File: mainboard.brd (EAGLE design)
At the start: 90.2 x 95.9 mm, 160 parts, among them IC1 LM234Z, J1 1981584-1, J2 POWER_JACKPTH_LOCK, Q1 IRLML5103, Q2 IRLML5103, Q3 IRLML5103, Q4 IRLML5103, Q5 IRLML5103, T1 NDS352A, T2 NDS352A, T3 NDS352A, T4 NDS352A, T5 NDS352A, U1 RFM23BP, U10 EP2W+, U11 S1216V8, U12 Value, U2 LSM9DS1, U3 MAX708RESA-T, U4 ATSAMD21G-A, U5 MAX4372TEUK+T, U6 MAX4372TEUK+T, U7 TPS54226PWPRPWP14_2P31X2P46-L, U8 LTC4121-4.2, U9 LC05111C13MTTTG, X1 BU-SMA-V, X2 BU-SMA-V, X3 BU-SMA-V, Y1 32.768kHz

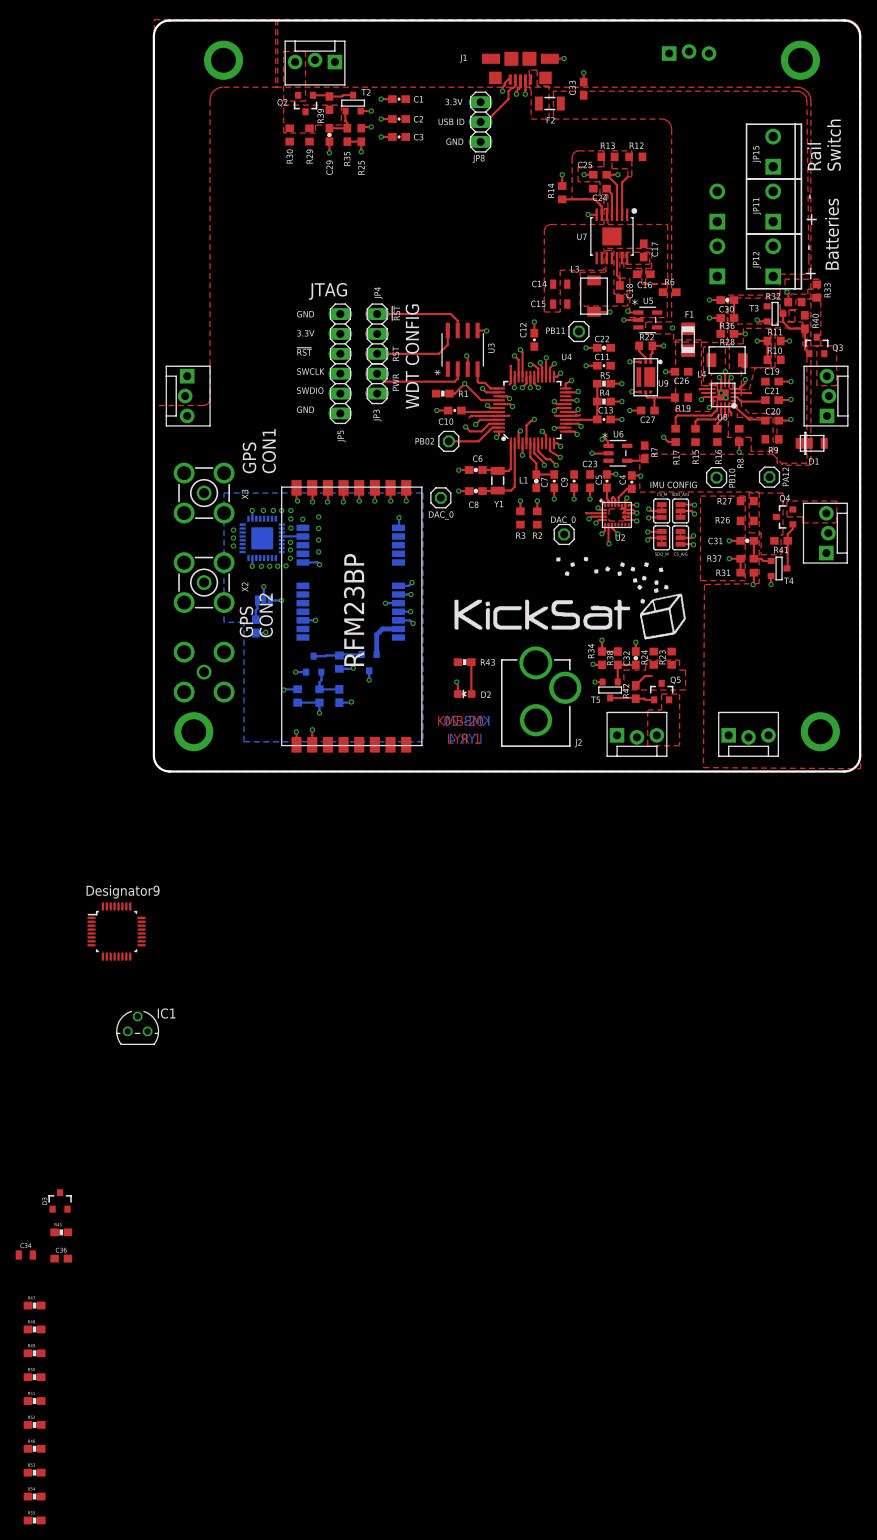
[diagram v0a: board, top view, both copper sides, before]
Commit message: Latest kicksat2 mainboard update (KMB-21). New from KMB-20: MRAM, power relays, microSD card, 2 spots for [XLab Tester Boards](https://github.com/maholli/XTB)
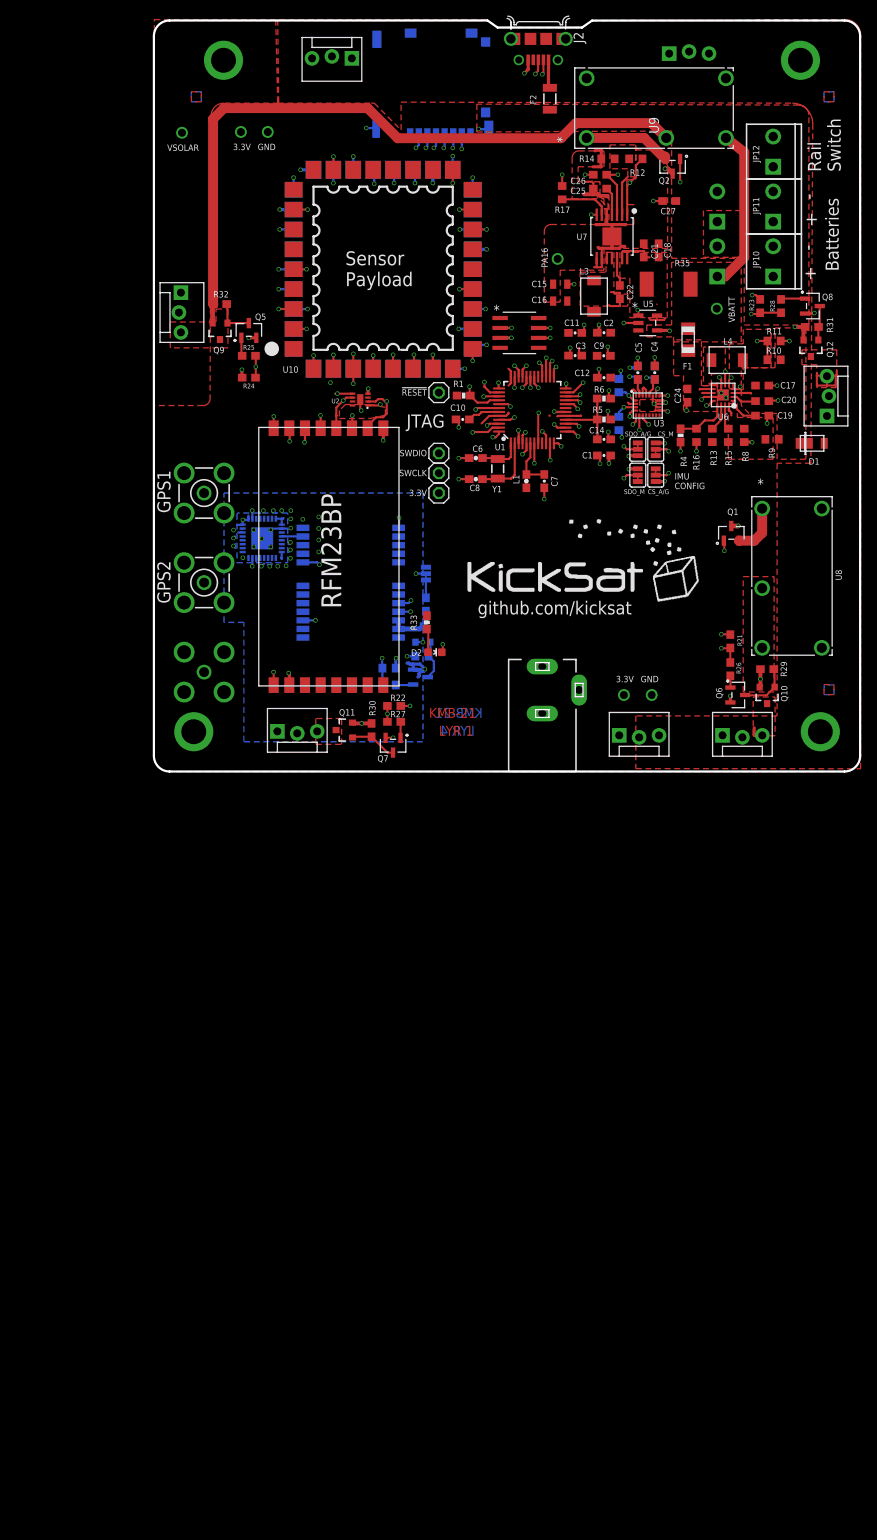
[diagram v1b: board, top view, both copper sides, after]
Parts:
- removed C28: 0.1uF, SparkFun-Capacitors:0603
- removed C29, C30, C31, C32: .1uF, SparkFun-Capacitors:0603-CAP@1
- removed C33: 2.2uF, SparkFun-Capacitors:0603
- removed C34: 0.33µF, SparkFun-Capacitors:0805
- removed C36: 10uF, SparkFun-Capacitors:0603
- removed D3: 200mA/70V, SparkFun-DiscreteSemi:SOT23-3
- removed IC1: LM234Z, linear:TO92
- removed JP18: M023.5MM_LOCK, SparkFun-Connectors:SCREWTERMINAL-3.5MM-2_LOCK
- removed JP19, JP20, JP21: (no value), SparkFun-Passives:PAD-JUMPER-3-2OF3_NC_BY_TRACE_YES_SILK_FULL_BOX
- removed JP22, JP28: (no value), pinhead:1X01
- removed JP7: (no value), SparkFun-Connectors:MOLEX-1X3_LOCK
- removed R36, R37, R38: 10k, SparkFun-Resistors:0603
- removed R39, R40, R41, R42: 3.3k, SparkFun-Resistors:0603
- removed R43, R45: 330, SparkFun-Resistors:0603-RES
- removed R44, R46, R47, R48, R49, R50, R51, R52, R53, R54, R55: 10K, SparkFun-Resistors:0603-RES
- removed R7: (no value), SparkFun-Resistors:0603
- removed T1, T2, T3, T4, T5: NDS352A, zetex:SOT-23
- added 3.3V: (no value), pinhead:1X01
- added J3: DCJ0303, maholli:DCJ0303
- added Q10, Q11, Q12, Q9: IRLML5103, User-Submitted:SOT23-3
- added Q6, Q7, Q8: IRLML2803, maholli:SOT-23
- added U13: RFM23BP, RFM23BP:RFM23BP
- added U14: S1216V8, maholli:S1216_24PIN_PACKAGE
- C14: value 22uF -> 0.1uF; device SparkFun-Capacitors:0805 -> SparkFun-Capacitors:0603-CAP
- C16: value 10uF -> 22uF; device SparkFun-Capacitors:0603 -> SparkFun-Capacitors:0805
- C18: value 1.0uF -> 10uF
- C19: value 10uF -> 2.2uF
- C20: value 2.2uF -> 2.2nF
- C21: value 2.2nF -> 10uF
- C22: value .1uF -> 0.1uF; device SparkFun-Capacitors:0603-CAP@1 -> SparkFun-Capacitors:0603
- C23: value 0.1uF -> .1uF; device SparkFun-Capacitors:0603 -> SparkFun-Capacitors:0603-CAP@1
- C24: value 3.3nF -> 22uF
- C25: value 1.0uF -> 3.3nF
- C26: value 22uF -> 1.0uF
- C27: value 0.1uF -> 2.2uF
- J1: value 1981584-1 -> 503182-1852; device audio amplifier example:1981584-1 -> maholli:MOLEX_503182-1852
- J2: value POWER_JACKPTH_LOCK -> 10118194-0001LF; device SparkFun-Connectors:POWER_JACK_PTH_LOCK -> 10118194-0001LF:FRAMATOME_10118194-0001LF
- JP10, JP13: value (none) -> M023.5MM_LOCK; device SparkFun-Connectors:MOLEX-1X3_LOCK -> SparkFun-Connectors:SCREWTERMINAL-3.5MM-2_LOCK
- JP15: value M023.5MM_LOCK -> (none); device SparkFun-Connectors:SCREWTERMINAL-3.5MM-2_LOCK -> SparkFun-Connectors:MOLEX-1X3_LOCK
- JP24: device pinhead:1X01 -> SparkFun-Passives:PAD-JUMPER-3-2OF3_NC_BY_TRACE_YES_SILK_FULL_BOX
- JP3: device pinhead:1X02 -> SparkFun-Passives:PAD-JUMPER-3-2OF3_NC_BY_TRACE_YES_SILK_FULL_BOX
- JP4: device pinhead:1X03 -> SparkFun-Passives:PAD-JUMPER-3-2OF3_NC_BY_TRACE_YES_SILK_FULL_BOX
- JP5: device pinhead:1X06 -> SparkFun-Connectors:MOLEX-1X3_LOCK
- JP8: device pinhead:1X03 -> SparkFun-Connectors:MOLEX-1X3_LOCK
- Q1, Q2, Q3, Q5: value IRLML5103 -> IRLML2803; device User-Submitted:SOT23-3 -> maholli:SOT-23
- R13: value 22.1 -> 470k
- R14: value 100K -> 22.1k
- R15: value 470k -> 4.7k
- R16: value 4.7k -> 6.04K
- R17: value 6.04K -> 100K
- R18: value 4.7K -> 10K
- R19: value 680 -> 4.7K
- R20: value 10K -> 3.3K
- R21: value 3.3K -> 10k; device resistor:R0603 -> SparkFun-Resistors:0603
- R22: value 1k -> 10k; device resistor:R0603 -> SparkFun-Resistors:0603
- R23, R24: value 4 -> 10k; device resistor:R0603 -> SparkFun-Resistors:0603
- R26, R27: value 4 -> 4.7k; device resistor:R0603 -> SparkFun-Resistors:0603
- R29, R30, R32: value 4 -> 100k; device resistor:R0603 -> SparkFun-Resistors:0603
- R31: value 4.7k -> 100k
- R33: value 4 -> 330; device resistor:R0603 -> SparkFun-Resistors:0603-RES
- R34: value 4.7k -> 10K; device SparkFun-Resistors:0603 -> SparkFun-Resistors:0603-RES
- R35: value 10k -> 0.025; device SparkFun-Resistors:0603 -> resistor:R2512
- R4: value 110K -> 10k
- R5: value 316K -> 110K
- R6: value (none) -> 316K; device SparkFun-Resistors:0603 -> SparkFun-Resistors:0603-RES
- U1: value RFM23BP -> MAX706R; device RFM23BP:RFM23BP -> maholli:SO8
- U10: value EP2W+ -> XTB_2018_04_25; device maholli:QFN32-5X5MM -> maholli:XTB_MEZ
- U11: value S1216V8 -> XTB_2018_04_25; device maholli:S1216_24PIN_PACKAGE -> maholli:XTB_MEZ
- U12: value Value -> EP2W+; device maholli:PBS0032A_N -> maholli:QFN32-5X5MM
- U2: value LSM9DS1 -> MR25H40; device SparkFun-Sensors:LGA24-8X4 -> maholli:DFN-8
- U3: value MAX708RESA-T -> LSM9DS1; device maholli:SO8 -> SparkFun-Sensors:LGA24-8X4
- U6: value MAX4372TEUK+T -> LTC4121-4.2; device maholli:21-0057F -> BrownSpaceEngineering:QFN-16-PAD
- U8: value LTC4121-4.2 -> PE014006; device BrownSpaceEngineering:QFN-16-PAD -> maholli:RELAY5-PE_CO
- U9: value LC05111C13MTTTG -> PE014006; device BrownSpaceEngineering:WDFN6 -> maholli:RELAY5-PE_CO
- moved FRAME1 128.9 mm to (-4.83, 87.1)
- moved FRAME2 128.9 mm to (-4.52, 78.2)
- moved FRAME3 128.9 mm to (-4.83, 60.5)
- moved FRAME4 128.9 mm to (-4.83, 69.3)
- moved J2 93.5 mm to (49.0, 93.5), turned to 180 degrees
- moved R29 89.8 mm to (78.2, 13.1), turned to 180 degrees
- moved JP8 84.3 mm to (72.5, 4.50), turned to 0 degrees
- moved R30 76.7 mm to (27.7, 5.30), turned to 90 degrees
- moved R32 73.4 mm to (8.38, 59.7)
- moved Q5 70.1 mm to (12.1, 56.4)
- moved Q3 65.9 mm to (34.0, 12.1), flipped to the bottom, turned to 90 degrees
- moved R33 65.3 mm to (34.8, 19.1)
- moved R24 62.9 mm to (12.1, 50.3), turned to 180 degrees
- moved JP5 62.6 mm to (86.0, 45.4), turned to 90 degrees
- moved R22 56.1 mm to (30.6, 8.38), turned to 0 degrees
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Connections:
- net PA04 renamed N$22
- removed net 3.3V_REF: U12.30
- removed net A_3.3V: U12.26
- removed net DAC_0: JP22.1, U4.3
- removed net GPS_PWR: Q1.2, U11.23
- removed net I_SOLAR: U4.13, U6.2
- removed net LED_GRN: D2.C, U4.7
- removed net N$22 (its old number): J2.GND, J2.GNDBREAK, JP11.2, JP12.2, JP15.1
- removed net N$27: R48.1, U12.6
- removed net N$41: C27.1, R19.1, U9.P$5
- removed net N$42: C17.1, U7.14
- removed net N$45: R22.2, U9.P$2
- removed net N$48: R51.1, U12.3
- removed net N$50: R46.1, U12.22
- removed net N$56: R55.1, U12.19
- removed net N_ENAB_REG: U4.25, U7.7
- removed net PA12: JP24.1, U4.21
- removed net PA15: U4.24
- removed net PB02: JP28.1, U4.47
- removed net PB09: JP27.1, U4.8
- removed net PB10: JP26.1, U4.19
- removed net PB11: JP25.1, U4.20
- removed net PB13: U4.22
- removed net PWR_GND: C14.1, C15.1, C16.2, C17.2, C24.2, C25.2, R13.1, U7.15, U7.5, U7.8, U7.9
- removed net SPI_SS: U1.NSEL, U4.41
- removed net SPI_SS2: U12.9
- removed net USB_D_N: J1.2, U4.33
- removed net USB_D_P: J1.3, U4.34
- removed net USB_ID: J1.4, JP8.2
- removed net VBURN_IN: Q2.3, Q3.3, Q4.3, Q5.3, R23.1, R24.1, R26.1, R27.1, R29.1, R30.1, R32.1, R33.1, R39.2, R40.2, R41.2, R42.2
- removed net WDT_!PFO: U3.5, U4.29
- removed net WDT_!RESET: JP4.1, U3.7
- removed net WDT_PFI: U3.4, U4.37
- removed net WDT_RESET: JP4.3, U3.8
- new net BURN_RELAY_A: Q2.1, U4.24
- new net BURN_RELAY_B: Q1.1, U4.15
- new net GPS_PWR_IN: Q4.3, R34.2, U14.22, U14.23
- new net LED_1: D2.C, U4.12
- new net SPI_CS_MRAM: U2.P$1
- new net SPI_CS_RFM: U13.NSEL, U4.41
- new net SPI_CS_SD: J1.2, U4.38
- new net SPI_CS_XTB1: U10.P$32, U4.39
- new net SPI_CS_XTB2: U11.P$32, U4.8
- new net USB_D+: J2.3, U4.34
- new net USB_D-: J2.2, U4.33
- new net VBATT_IN: C27.1, F2.2, JP10.1, JP11.1, JP13.2
- new net VBURN_A_IN: Q12.2, Q9.2, R31.2, R32.2, U9.11
- new net VBURN_B_IN: Q10.2, Q11.2, R29.2, R30.2, U8.11
- new net WDT_PWR: U1.2
- new net WDT_WDI: U1.6, U4.28
- new net XTB_RESET: U10.P$26, U11.P$26, U4.37
- new net XTB_START: U10.P$33, U11.P$33, U4.47
- net !RESET: now also JP27.1, U1.7; no longer JP4.2, JP5.3
- net 3.3V: now also 3.3V.1, C13.1, C16.2, J1.4, JP3.3, JP4.3, Q4.2, R13.2, R20.1, U10.P$1, U10.P$18, U10.P$20, U10.P$24, U10.P$27, U10.P$3, U10.P$6, U10.P$7, U11.P$1, U11.P$18, U11.P$20, U11.P$24, U11.P$27, U11.P$3, U11.P$6, U11.P$7, U13.VCC, U3.1, U3.22, U3.23, U3.3; no longer C14.2, C22.1, JP20.3, JP21.3, JP3.2, JP5.2, JP8.1, Q1.3, R16.2, R21.1, R23.2, R24.2, R26.2, R27.2, R29.2, R30.2, R32.2, R43.2, R44.2, R7.1, U1.VCC, U11.22, U12.15, U12.16, U2.1, U2.22, U2.23, U2.3, U6.3, U6.5
- net ENAB_BURN1: now also R24.1, U4.48; no longer R35.1, U4.38
- net ENAB_BURN2: now also R23.1; no longer R36.1
- net ENAB_BURN3: now also R22.1, R27.2, U4.14; no longer R31.2, R37.1, U4.11
- net ENAB_BURN4: now also R21.1, R26.2, U4.13; no longer R34.2, R38.1, U4.12
- net ENAB_GPS: now also R19.1, U4.11; no longer R20.2, U4.39
- net GND: now also C14.2, C15.1, C16.1, C17.2, C18.2, C21.2, C24.2, C25.2, J1.6, J1.P1, J1.P2, J1.P3, J1.P4, J1.P5, J2.5, JP12.2, JP15.1, JP24.1, JP3.1, JP4.1, JP8.1, Q3.2, Q5.2, Q6.2, Q7.2, Q8.2, R14.1, R16.1, R21.2, R22.2, R23.2, R24.2, R5.1, U1.3, U10.P$11, U10.P$17, U10.P$19, U10.P$2, U10.P$23, U10.P$28, U10.P$34, U10.P$5, U10.P$8, U11.P$11, U11.P$17, U11.P$19, U11.P$2, U11.P$23, U11.P$28, U11.P$34, U11.P$5, U11.P$8, U12.1, U12.10, U12.11, U12.12, U12.13, U12.16, U12.18, U12.19, U12.2, U12.20, U12.21, U12.22, U12.23, U12.25, U12.3, U12.30, U12.31, U12.32, U12.5, U12.6, U12.7, U12.9, U12.EP, U13.GND1, U13.GND2, U13.GND3, U14.10, U14.12, U14.13, U14.24, U2.P$4, U2.P$9, U3.14, U3.15, U3.16, U3.17, U3.18, U3.19, U3.20, U6.P$11, U6.P$12, U6.P$17, U6.P$5, U6.P$7, U7.15, U7.5, U7.8, U7.9, U8.12, U8.5, U9.12, U9.5; no longer C20.2, C22.2, C28.2, C29.2, C30.2, C31.2, C32.2, C33.2, C34.1, C34.2, C36.1, J1.5, J1.S1, JP10.1, JP13.1, JP15.2, JP19.1, JP20.1, JP21.1, JP5.6, JP7.1, JP8.3, R17.1, R22.1, R25.1, R28.1, R31.1, R34.1, R4.1, T1.2, T2.2, T3.2, T4.2, T5.2, U1.GND1, U1.GND2, U1.GND3, U10.1, U10.10, U10.11, U10.12, U10.13, U10.14, U10.16, U10.17, U10.18, U10.19, U10.2, U10.20, U10.21, U10.22, U10.23, U10.24, U10.25, U10.27, U10.28, U10.29, U10.3, U10.30, U10.31, U10.32, U10.5, U10.6, U10.7, U10.8, U10.9, U10.EP, U11.10, U11.12, U11.13, U11.24, U2.14, U2.15, U2.16, U2.17, U2.18, U2.19, U2.20, U3.3, U6.1, U8.P$11, U8.P$12, U8.P$17, U8.P$5, U8.P$7, U9.P$1, U9.P$3, U9.P$4
- net GPS_1PPS: now also U14.3, U4.7; no longer U11.3, U4.4
- net I2C_SCL: now also R3.1, U3.2, U4.22; no longer R2.1, U11.19, U2.2, U4.15
- net I2C_SDA: now also R2.1, U3.4, U4.21; no longer R3.1, U11.18, U2.4, U4.14
- net I2C_SDOA/G: now also JP2.2, U3.5; no longer JP1.2, U2.5
- net L1_CHG: now also U6.P$16; no longer U8.P$16
- net L1_FAULTN: now also R15.1, U6.P$15; no longer R16.1, U8.P$15
- net L1_PROG: now also R16.2, R4.1, U6.P$13; no longer R17.2, U8.P$13
- net LION1: now also C24.1, U6.P$10, U6.P$9; no longer C26.1, R19.2, U8.P$10, U8.P$9
- net N$1: now also R33.1; no longer R43.1
- net N$10: now also Q3.1, R19.2; no longer C28.1, R20.1, T1.3
- net N$11: now also Q5.1, R25.1; no longer C31.1, R37.2, T4.3
- net N$12: now also Q3.3, Q4.1, R20.2; no longer Q1.1, R21.2, T1.1
- net N$13: now also C14.1, R5.2, R6.1, U4.16; no longer F2.1, J1.1
- net N$14: now also C22.2; no longer C18.2
- net N$15: now also Q12.1, Q8.3, R31.1; no longer Q3.1, R40.1, T3.1
- net N$16: now also U12.15; no longer U10.15
- net N$17: now also U12.26, X1.1; no longer U10.26, X3.1
- net N$19: now also U13.ANT, X3.1; no longer U1.ANT, X1.1
- net N$2: now also U3.21; no longer U2.21
- net N$20: now also F2.1, J2.1; no longer R47.1, U12.7
- net N$21: now also JP1.2, U3.6; no longer JP2.2, U2.6
- net N$23: now also JP3.2, U3.8; no longer JP20.2, U2.8
- net N$24: now also JP24.3, R34.1; no longer JP19.3, R44.1
- net N$25: now also Q8.1, R28.1; no longer C29.1, R35.2, T2.3
- net N$26: now also JP4.2, U3.7; no longer JP21.2, U2.7
- net N$3: now also C22.1; no longer C18.1
- net N$30: now also Q7.1, R27.1; no longer R49.1, U12.5
- net N$31: now also U2.P$3; no longer IC1.2, R45.2
- net N$32: now also C20.2, U6.P$4; no longer C21.2, U8.P$4
- net N$33: now also C20.1, U6.P$2; no longer C21.1, U8.P$2
- net N$34: now also C19.1, U6.P$1; no longer C20.1, U8.P$1
- net N$35: now also U6.P$6; no longer U8.P$6
- net N$36: now also U6.P$8; no longer U8.P$8
- net N$37: now also R13.1, U6.P$14; no longer R15.1, U8.P$14
- net N$38: now also Q2.2, U9.1; no longer C32.1, R38.2, T5.3
- net N$39: now also U2.P$8; no longer D3.1, IC1.3, R45.1
- net N$4: now also JP13.1, JP16.2; no longer JP16.1, JP18.2
- net N$40: now also Q1.2, U8.1; no longer C13.1, R4.2, R5.1, U4.16
- net N$43: now also J3.2, J3.3, JP10.2, JP11.2, JP12.1; no longer R50.1, U12.4
- net N$44: now also Q11.1, Q7.3, R30.1; no longer Q4.1, R41.1, T4.1
- net N$46: now also C26.1, R17.2; no longer C25.1, R14.2
- net N$47: now also Q10.1, Q6.3, R29.1; no longer Q5.1, R42.1, T5.1
- net N$49: now also U2.P$7; no longer R52.1, U12.2
- net N$5: now also Q6.1, R26.1; no longer C30.1, R36.2, T3.3
- net N$51: now also C25.1; no longer C24.1
- net N$52: now also R14.2; no longer R13.2
- net N$53: now also U4.29; no longer R53.1, U12.21
- net N$54: now also U4.25; no longer C36.2, U12.23
- net N$55: now also U4.19; no longer R54.1, U12.20
- net N$6: now also U3.24; no longer U2.24
- net N$7: now also Q5.3, Q9.1, R32.1; no longer Q2.1, R39.1, T2.1
- net N$8: now also R4.2, U4.20; no longer JP3.1, U3.2
- net N$9: now also JP24.2, U14.8; no longer JP19.2, U11.8
- net PGOOD: now also R17.1; no longer R14.1
- net RF_IN: now also U12.4, U14.11; no longer U10.4, U11.11
- net RF_NIRQ: now also U13.NIRQ, U4.3; no longer U1.NIRQ, U4.48
- net RF_SDN: now also U13.SDN, U4.4; no longer U1.SDN, U4.28
- net SPI_MISO: now also J1.7, U10.P$29, U11.P$29, U13.SDO, U2.P$2; no longer U1.SDO, U12.10, U12.12
- net SPI_MOSI: now also J1.3, U10.P$31, U11.P$31, U13.SDI, U2.P$5; no longer U1.SDI
- net SPI_SCK: now also J1.5, U10.P$30, U11.P$30, U13.SCK, U2.P$6; no longer U1.SCK, U12.11
- net SWCLK: now also JP26.1; no longer JP5.4
- net SWDIO: now also JP25.1; no longer JP5.5
- net UART1_RX: now also U14.20; no longer U11.20
- net UART1_TX: now also U14.21; no longer U11.21
- net VBATT: now also J3.1, JP16.1, Q1.3, Q2.3, R35.2, U7.7, U8.14, U9.14; no longer C33.1, F2.2, J2.PWR, JP11.1, JP12.1, JP16.2, JP18.1, R5.2
- net VBURN1: now also Q9.3; no longer Q2.2
- net VBURN2: now also JP5.3, Q12.3; no longer JP7.3, Q3.2
- net VBURN3: now also JP9.3, Q11.3; no longer JP10.3, Q4.2
- net VBURN4: now also JP8.3, Q10.3; no longer JP9.3, Q5.2
- net VREG_IN: now also C18.1, C21.1, R35.1, U7.14; no longer C16.1, R6.1
- net VSOLAR: now also JP15.2, JP5.2, JP9.2; no longer JP10.2, JP13.2, JP7.2, R7.2, U6.4
- net VSOLAR_IN: now also C17.1, U6.P$3; no longer C19.1, U8.P$3
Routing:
- net VBURN_A_IN: track 0.00 -> 123.7 mm, vias 0 -> 1
- net N$22 (its old number): track 103.8 -> 0.00 mm
- net N$43: track 0.00 -> 94.4 mm
- net SPI_CS_XTB2: track 0.00 -> 77.9 mm, vias 0 -> 2
- net XTB_START: track 0.00 -> 59.3 mm, vias 0 -> 3
- net VBATT: track 97.5 -> 155.9 mm, vias 2 -> 6
- net VBURN_B_IN: track 0.00 -> 58.3 mm, vias 0 -> 2
- net GND: track 110.2 -> 156.8 mm, vias 95 -> 115
- net I2C_SDA: track 57.3 -> 10.9 mm, vias 4 -> 2
- net SPI_MOSI: track 32.8 -> 79.0 mm, vias 2 -> 6
- net SPI_SCK: track 32.1 -> 77.3 mm, vias 2 -> 5
- net SPI_CS_SD: track 0.00 -> 42.8 mm, vias 0 -> 2
- net VSOLAR: track 2.71 -> 45.2 mm, vias 0 -> 1
- net I2C_SCL: track 53.6 -> 11.2 mm, vias 4 -> 2
- net SPI_MISO: track 30.4 -> 72.6 mm, vias 2 -> 5
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- added copper zone on layer 16, net N$27
- added copper zone on layer 1, net N$4
- added copper zone on layer 16, net N$41
- added copper zone on layer 16, net N$42
- added copper zone on layer 15, net N$43
- added copper zone on layer 1, net N$45
- added copper zone on layer 1, net N$48
- added copper zone on layer 1, net N$50
- added copper zone on layer 1, net VBATT_IN
- added copper zone on layer 1, net VBURN_B_IN
- removed copper zone on layer 1, net N$13
- removed copper zone on layer 15, net N$22 (its old number)
- removed copper zone on layer 15, net N$4
- removed copper zone on layer 1, net N$42
- removed copper zone on layer 1, net N$5
- removed copper zone on layer 1, net PWR_GND
- removed copper zone on layer 15, net VBATT
- removed copper zone on layer 1, net VBURN_IN
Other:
- outline, holes or cut-outs redrawn
- board text added: "!RESET"
- board text added: "1"
- board text added: "2"
- board text added: "Footswitch"
- board text added: "GPS1"
- board text added: "GPS2"
- board text added: "KMB-21"
- board text added: "PA16"
- board text added: "RADIO"
- board text added: "SWCLK"
- board text added: "SWDIO"
- board text added: "Sensor Payload"
- board text added: "VBATT"
- board text added: "VSOLAR"
- board text added: "github.com/kicksat"
- board text removed: "!RST"
- board text removed: "DAC_0"
- board text removed: "GND 3.3V !RST SWCLK SWDIO GND"
- board text removed: "GPS CON1"
- board text removed: "GPS CON2"
- board text removed: "KMB-20"
- board text removed: "PA12"
- board text removed: "PB02"
- board text removed: "PB10"
- board text removed: "PB11"
- board text removed: "PWR"
- board text removed: "RFM23 CONNECTOR"
- board text removed: "RST"
- board text removed: "USB ID"
- board text removed: "WDT CONFIG"
